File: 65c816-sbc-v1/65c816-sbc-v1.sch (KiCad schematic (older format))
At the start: 13 parts, among them U1 W65C816SxP, U10 W65C22SxP, U2 74HC573, U3 74HC245, U4 PAL20L8, U5 PAL20L8, U6 74HC244, U7 74HC244, U8 AS6C4008-55PCN, U9 28C256

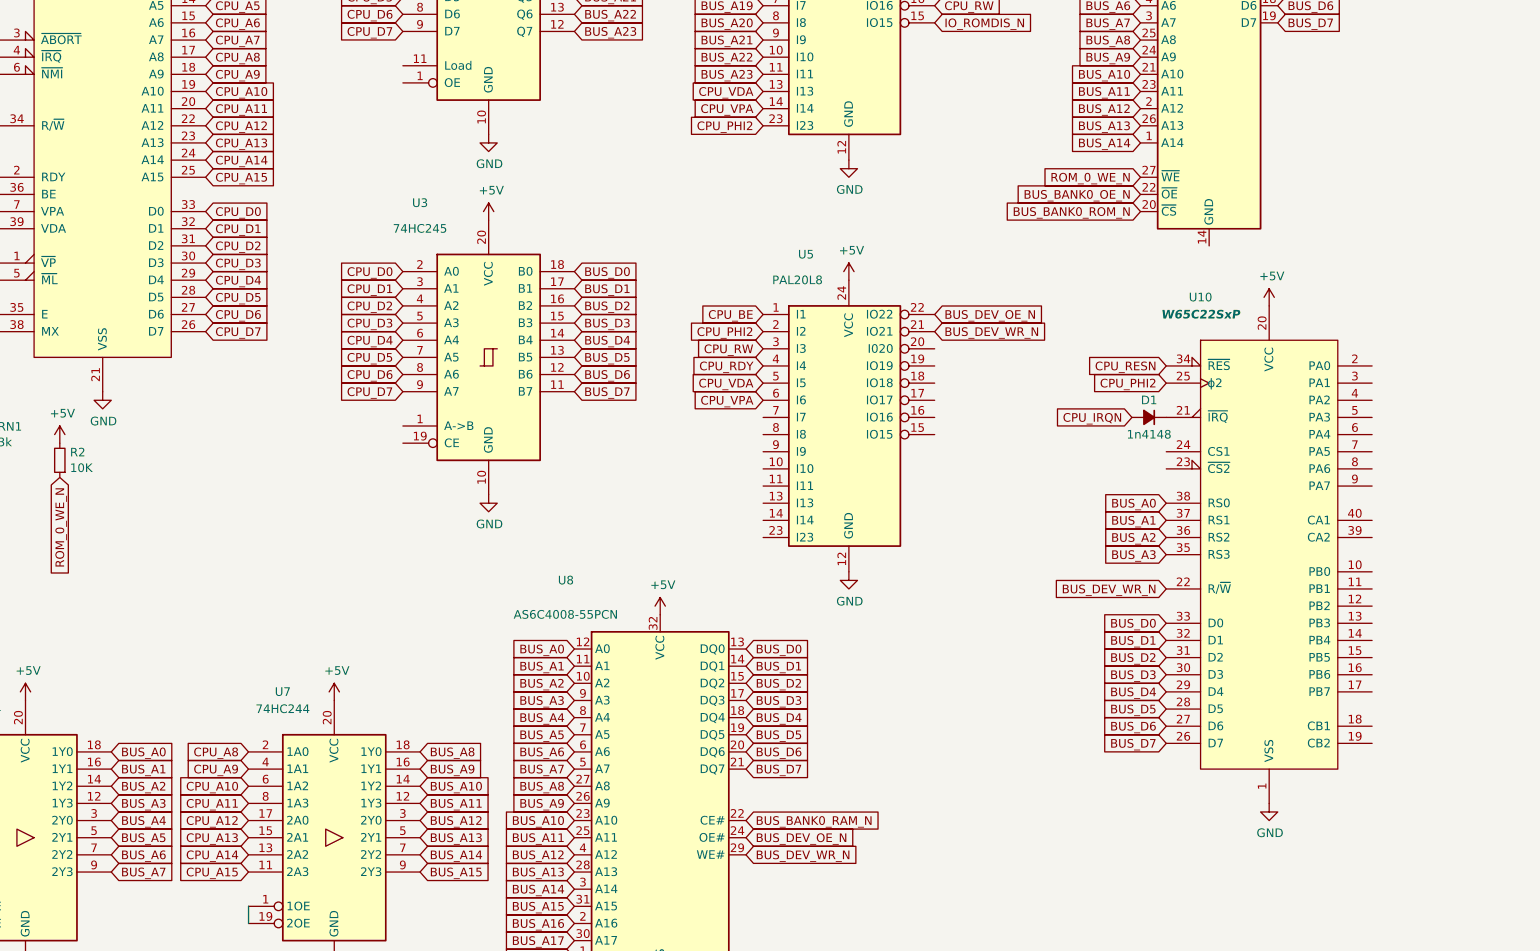
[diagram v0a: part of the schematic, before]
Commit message: squeeze in an ACIA too
It's half done, and I still need to figur eout how to do the two CS'es
on these peripherals given my current IO decoding scheme.
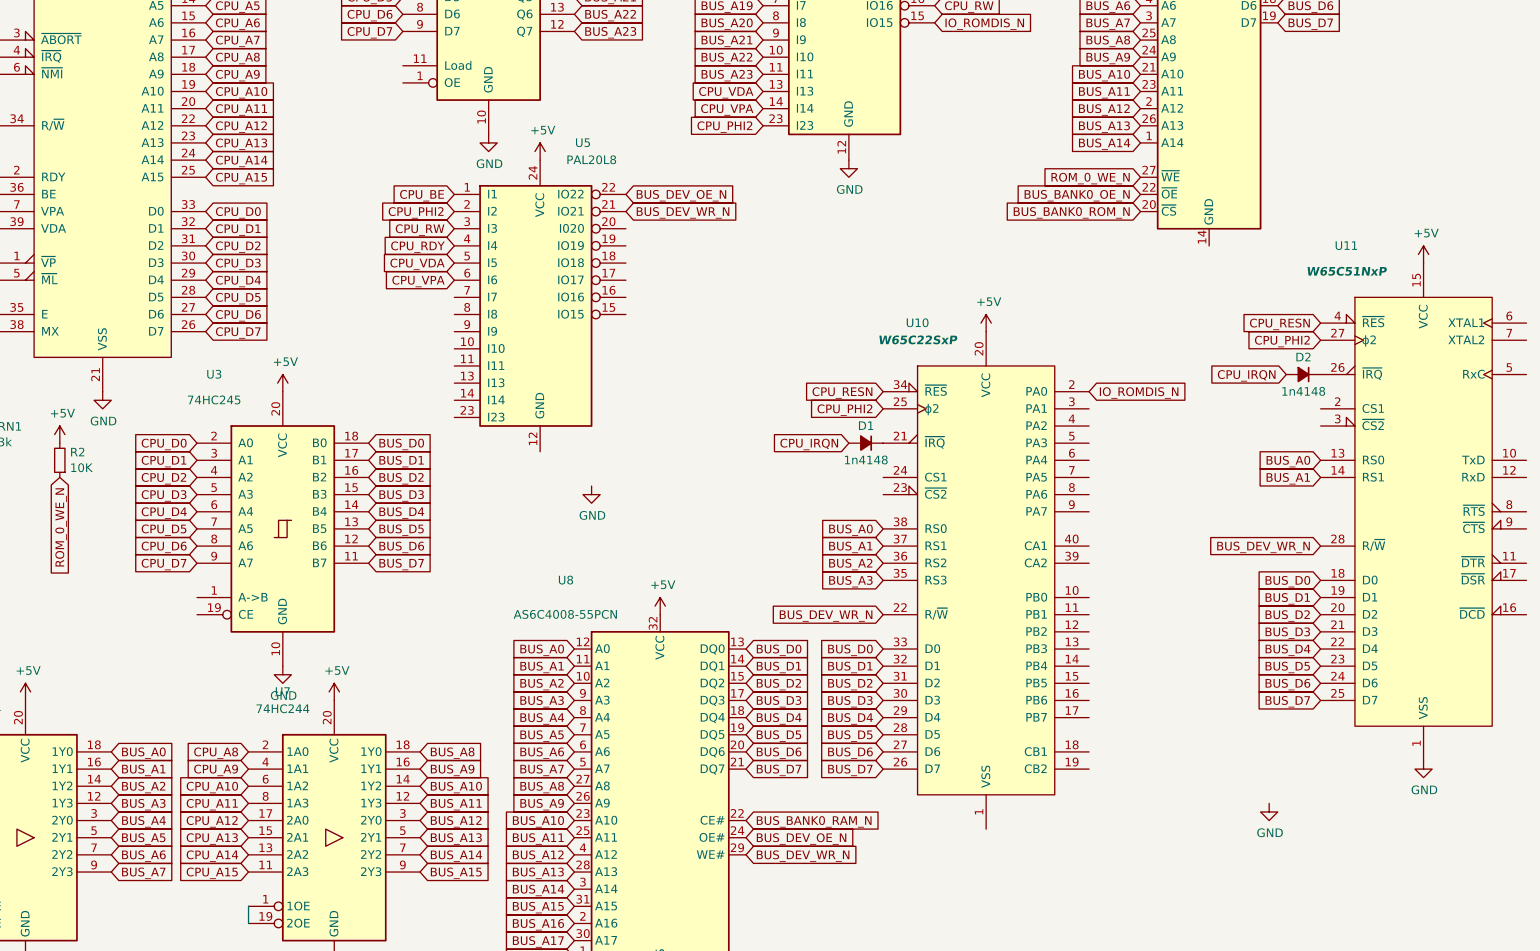
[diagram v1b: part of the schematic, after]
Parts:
- added D2: 1n4148, symbol Device:D_Small_ALT
- added U11: W65C51NxP, symbol 65xx:W65C51NxP
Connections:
- net +5V: now also U11.15 (VCC)
- net BUS_A0: now also U11.13 (RS0)
- net BUS_A1: now also U11.14 (RS1)
- net BUS_D0: now also U11.18 (D0)
- net BUS_D1: now also U11.19 (D1)
- net BUS_D2: now also U11.20 (D2)
- net BUS_D3: now also U11.21 (D3)
- net BUS_D4: now also U11.22 (D4)
- net BUS_D5: now also U11.23 (D5)
- net BUS_D6: now also U11.24 (D6)
- net BUS_D7: now also U11.25 (D7)
- net BUS_DEV_WR_N: now also U11.28 (R/~W)
- net CPU_IRQN: now also D2.2 (A)
- net CPU_PHI2: now also U11.27 (ϕ2)
- net CPU_RESN: now also U11.4 (~RES)
- net GND: now also U11.1 (VSS); no longer U10.1 (VSS), U5.12 (GND)
- net IO_ROMDIS_N: now also U10.2 (PA0)
- new net: D2.1 (K), U11.26 (~IRQ)
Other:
- moved on the sheet: D1, U10, U3, U5

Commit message: Update larger layout, more IO pins defined
Still need to do clock, reset sequencing, etc.
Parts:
- added C1: 30pF, symbol Device:C_Small
- added R3: 1M, symbol Device:R_Small
- added U12: 74HC138, symbol 74xx:74LS138
- added Y1: 1.8432MHz, symbol Device:Crystal
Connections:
- net +5V: now also U9.28 (VCC), U12.16 (VCC); no longer U3.20 (VCC)
- net BUS_A4: now also U12.1 (A0)
- net BUS_A5: now also U12.2 (A1)
- net BUS_A6: now also U12.3 (A2)
- net BUS_A7: now also U12.6 (E3)
- net BUS_A8: now also U12.5 (E2)
- net BUS_BANK0_IO_N: now also U12.4 (E1)
- net GND: now also U10.1 (VSS), U5.12 (GND), U9.14 (GND), C1.2, U12.8 (GND)
- net BUS_DA_LATCH_OE_N: now reaches U2.1 (OE)
- net BUS_DA_LATCH_OE_N: now also U3.19 (CE), U5.15 (IO15), U6.1 (1OE), U6.19 (2OE), U7.1 (1OE), U7.19 (2OE)
- net BUS_DA_LATCH_LE: now reaches U2.11 (Load)
- net BUS_DA_LATCH_LE: now also U5.16 (IO16)
- net BUS_DA_LATCH_DIR: now reaches U3.1 (A->B)
- net BUS_DA_LATCH_DIR: now also U5.17 (IO17)
- net BUS_IO_DEVICE_EN: now reaches U11.2 (CS1)
- net BUS_IO_DEVICE_EN: now also U10.24 (CS1), U5.20 (I020)
- net IO_CSEN_0_N: now reaches U11.3 (~CS2)
- net IO_CSEN_0_N: now also U12.15 (O0)
- net ACIA_XTAL1: now reaches U11.6 (XTAL1)
- net ACIA_XTAL1: now also R3.1, Y1.1
- net ACIA_XTAL2: now reaches U11.7 (XTAL2)
- net ACIA_XTAL2: now also C1.1, R3.2, Y1.2
- net IO_CSEN_1_N: now reaches U10.23 (~CS2)
- net IO_CSEN_1_N: now also U12.14 (O1)
- new net IO_CSEN_2_N: U12.13 (O2)
- new net IO_CSEN_3_N: U12.12 (O3)
- new net IO_CSEN_4_N: U12.11 (O4)
- new net IO_CSEN_5_N: U12.10 (O5)
- new net IO_CSEN_6_N: U12.9 (O6)
- new net IO_CSEN_7_N: U12.7 (O7)
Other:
- moved on the sheet: D1, D2, R2, RN1, U10, U11, U2, U3, U4, U5, U6, U7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

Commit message: starting to play around with buttons
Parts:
- added C3: 1uF, symbol Device:C_Small
- added D3: 1N4148, symbol Device:D_Small
- added R8: 2M, symbol Device:R_Small
- added SW1: RESET, symbol Switch:SW_Push
- added SW2: NMI, symbol Switch:SW_Push
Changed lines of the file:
@@
 Text GLabel 12050 6050 0    50   Input ~ 0
 BUS_IO_DEVICE_EN
+$Comp
+L Device:D_Small D3
+U 1 1 61DCFAE9
+P 14000 3950
+F 0 "D3" H 14000 4157 50  0000 C CNN
+F 1 "1N4148" H 14000 4066 50  0000 C CNN
+F 2 "" V 14000 3950 50  0001 C CNN
+F 3 "~" V 14000 3950 50  0001 C CNN
+	1    14000 3950
+	1    0    0    -1
+$EndComp
+$Comp
+L Device:R_Small R8
+U 1 1 61DD0317
+P 14000 4300
+F 0 "R8" V 14196 4300 50  0000 C CNN
+F 1 "2M" V 14105 4300 50  0000 C CNN
+F 2 "" H 14000 4300 50  0001 C CNN
+F 3 "~" H 14000 4300 50  0001 C CNN
+	1    14000 4300
+	0    -1   -1   0
+$EndComp
+$Comp
+L Device:C_Small C3
+U 1 1 61DD0F01
+P 14450 4050
+F 0 "C3" H 14542 4096 50  0000 L CNN
+F 1 "1uF" H 14542 4005 50  0000 L CNN
+F 2 "" H 14450 4050 50  0001 C CNN
+F 3 "~" H 14450 4050 50  0001 C CNN
+	1    14450 4050
+	1    0    0    -1
+$EndComp
+$Comp
+L Switch:SW_Push SW1
+U 1 1 61DD2E7B
+P 15500 4400
+F 0 "SW1" H 15500 4685 50  0000 C CNN
+F 1 "RESET" H 15500 4594 50  0000 C CNN
+F 2 "" H 15500 4600 50  0001 C CNN
+F 3 "~" H 15500 4600 50  0001 C CNN
+	1    15500 4400
+	1    0    0    -1
+$EndComp
+$Comp
+L Switch:SW_Push SW2
+U 1 1 61DD3596
+P 15450 4850
+F 0 "SW2" H 15450 5135 50  0000 C CNN
+F 1 "NMI" H 15450 5044 50  0000 C CNN
+F 2 "" H 15450 5050 50  0001 C CNN
+F 3 "~" H 15450 5050 50  0001 C CNN
+	1    15450 4850
+	1    0    0    -1
+$EndComp
 $EndSCHEMATC

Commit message: More routing!
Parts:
- added C20, C21, C22, C23, C24, C25, C26, C27, C28, C29, C30, C31: 0.1u, symbol Device:C_Small
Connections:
- net +5V: now also U3.20 (VCC), C20.1, C21.1, C22.1, C23.1, C24.1, C25.1, C26.1, C27.1, C28.1, C29.1, C30.1, C31.1
- net GND: now also C20.2, C21.2, C22.2, C23.2, C24.2, C25.2, C26.2, C27.2, C28.2, C29.2, C30.2, C31.2
- net ACIA_TXD: now reaches U11.10 (TxD)
- net ACIA_DTR: now reaches U11.11 (~DTR)
- net ACIA_RXD: now reaches U11.12 (RxD)
- net ACIA_DCD: now reaches U11.16 (~DCD)
- net ACIA_DSR: now reaches U11.17 (~DSR)
- net ACIA_RXC: now reaches U11.5 (RxC)
- net ACIA_RTS: now reaches U11.8 (~RTS)
- net ACIA_CTS: now reaches U11.9 (~CTS)
- net VIA_PB0: now reaches U10.10 (PB0)
- net VIA_PB1: now reaches U10.11 (PB1)
- net VIA_PB2: now reaches U10.12 (PB2)
- net VIA_PB3: now reaches U10.13 (PB3)
- net VIA_PB4: now reaches U10.14 (PB4)
- net VIA_PB5: now reaches U10.15 (PB5)
- net VIA_PB6: now reaches U10.16 (PB6)
- net VIA_PB7: now reaches U10.17 (PB7)
- net VIA_CB1: now reaches U10.18 (CB1)
- net VIA_CB2: now reaches U10.19 (CB2)
- net VIA_PA1: now reaches U10.3 (PA1)
- net VIA_CA2: now reaches U10.39 (CA2)
- net VIA_PA2: now reaches U10.4 (PA2)
- net VIA_CA1: now reaches U10.40 (CA1)
- net VIA_PA3: now reaches U10.5 (PA3)
- net VIA_PA4: now reaches U10.6 (PA4)
- net VIA_PA5: now reaches U10.7 (PA5)
- net VIA_PA6: now reaches U10.8 (PA6)
- net VIA_PA7: now reaches U10.9 (PA7)

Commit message: * update * add some microchip/AVR GAL symbols to maybe start using
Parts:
- added J1: EXPANSION, symbol Connector_Generic:Conn_02x20_Counter_Clockwise
- added J2: SIO, symbol Connector_Generic:Conn_02x10_Counter_Clockwise
- added J3: VIA_A, symbol Connector:Conn_01x10_Male
- added J4: VIA_B, symbol Connector:Conn_01x10_Male
- added U15: 74HC74, symbol 74xx:74HC74
- added X1: 28MHz, Oscillator:Oscillator_DIP-14, symbol Oscillator:CXO_DIP14
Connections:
- net +5V: now also J1.1 (Pin_1), J2.1 (Pin_1), U15.1 (~R), U15.14 (VCC), U15.4 (~S), X1.14 (Vcc)
- net ACIA_CTS: now also J2.16 (Pin_16)
- net ACIA_DCD: now also J2.13 (Pin_13)
- net ACIA_DSR: now also J2.14 (Pin_14)
- net ACIA_DTR: now also J2.15 (Pin_15)
- net ACIA_RTS: now also J2.17 (Pin_17)
- net ACIA_RXD: now also J2.18 (Pin_18)
- net ACIA_TXD: now also J2.19 (Pin_19)
- net BUS_A0: now also J1.2 (Pin_2)
- net BUS_A1: now also J1.3 (Pin_3)
- net BUS_A10: now also J1.12 (Pin_12)
- net BUS_A11: now also J1.13 (Pin_13)
- net BUS_A12: now also J1.14 (Pin_14)
- net BUS_A13: now also U4.2 (I2), J1.15 (Pin_15); no longer U4.1 (I1)
- net BUS_A14: now also U4.3 (I3), J1.16 (Pin_16); no longer U4.2 (I2)
- net BUS_A15: now also U4.4 (I4), J1.17 (Pin_17); no longer U4.3 (I3)
- net BUS_A16: now also U4.5 (I5), J1.18 (Pin_18); no longer U4.4 (I4)
- net BUS_A17: now also U4.6 (I6), J1.19 (Pin_19); no longer U4.5 (I5)
- net BUS_A18: now also U4.7 (I7), J1.20 (Pin_20); no longer U4.6 (I6)
- net BUS_A19: now also U4.8 (I8), J1.21 (Pin_21); no longer U4.7 (I7)
- net BUS_A2: now also J1.4 (Pin_4)
- net BUS_A20: now also U4.9 (I9), J1.22 (Pin_22); no longer U4.8 (I8)
- net BUS_A21: now also U4.10 (I10), J1.23 (Pin_23); no longer U4.9 (I9)
- net BUS_A22: now also U4.11 (I11), J1.24 (Pin_24); no longer U4.10 (I10)
- net BUS_A23: now also U4.13 (I13), J1.25 (Pin_25); no longer U4.11 (I11)
- net BUS_A3: now also J1.5 (Pin_5)
- net BUS_A4: now also J1.6 (Pin_6)
- net BUS_A5: now also J1.7 (Pin_7)
- net BUS_A6: now also J1.8 (Pin_8)
- net BUS_A7: now also J1.9 (Pin_9)
- net BUS_A8: now also J1.10 (Pin_10)
- net BUS_A9: now also J1.11 (Pin_11)
- net BUS_D0: now also J1.36 (Pin_36)
- net BUS_D1: now also J1.35 (Pin_35)
- net BUS_D2: now also J1.34 (Pin_34)
- net BUS_D3: now also J1.33 (Pin_33)
- net BUS_D4: now also J1.32 (Pin_32)
- net BUS_D5: now also J1.31 (Pin_31)
- net BUS_D6: now also J1.30 (Pin_30)
- net BUS_D7: now also J1.29 (Pin_29)
- net BUS_DEV_OE_N: now also J1.28 (Pin_28)
- net BUS_DEV_WR_N: now also J1.27 (Pin_27)
- net CPU_BE: now also U5.2 (I2); no longer U5.1 (I1)
- net CPU_PHI2: now also U4.1 (I1), U5.1 (I1), J1.38 (Pin_38), U15.5 (Q); no longer U4.23 (I23), U5.2 (I2)
- net CPU_RESN: now also J1.37 (Pin_37), J2.11 (Pin_11)
- net CPU_VDA: now also U4.14 (I14); no longer U4.13 (I13)
- net CPU_VPA: now also U4.23 (I23); no longer U4.14 (I14)
- net GND: now also J1.40 (Pin_40), J2.20 (Pin_20), U15.7 (GND), X1.7 (GND)
- net IO_ROMDIS_N: now also J3.1 (Pin_1)
- net VIA_CA1: now also J3.9 (Pin_9)
- net VIA_CA2: now also J3.10 (Pin_10)
- net VIA_CB1: now also J4.9 (Pin_9)
- net VIA_CB2: now also J4.10 (Pin_10)
- net VIA_PA1: now also J3.2 (Pin_2)
- net VIA_PA2: now also J3.3 (Pin_3)
- net VIA_PA3: now also J3.4 (Pin_4)
- net VIA_PA4: now also J3.5 (Pin_5)
- net VIA_PA5: now also J3.6 (Pin_6)
- net VIA_PA6: now also J3.7 (Pin_7)
- net VIA_PA7: now also J3.8 (Pin_8)
- net VIA_PB0: now also J4.1 (Pin_1)
- net VIA_PB1: now also J4.2 (Pin_2)
- net VIA_PB2: now also J4.3 (Pin_3)
- net VIA_PB3: now also J4.4 (Pin_4)
- net VIA_PB4: now also J4.5 (Pin_5)
- net VIA_PB5: now also J4.6 (Pin_6)
- net VIA_PB6: now also J4.7 (Pin_7)
- net VIA_PB7: now also J4.8 (Pin_8)
- new net: U15.3 (C), X1.8 (OUT)
- new net BUS_A24: J1.26 (Pin_26)
- new net CPU_PHI1: J1.39 (Pin_39), U15.2 (D), U15.6 (~Q)
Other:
- moved on the sheet: D1, U10, U8

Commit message: update!
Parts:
- added C32, C33, C34, C35, C36, C37: 0.1u, symbol Device:C_Small
- added C38: 33uF, symbol Device:CP
- added J5: power, symbol Connector:Conn_01x02_Male
- D1, D2, D3: footprint (none) -> Diode_THT:D_DO-35_SOD27_P7.62mm_Horizontal
- J1: footprint (none) -> Connector_PinHeader_2.54mm:PinHeader_2x20_P2.54mm_Vertical
- J2: footprint (none) -> Connector_PinHeader_2.54mm:PinHeader_2x10_P2.54mm_Vertical
- J3, J4: footprint (none) -> Connector_PinHeader_2.54mm:PinHeader_1x10_P2.54mm_Vertical
- U1, U10, U11: footprint (none) -> Package_DIP:DIP-40_W25.4mm_Socket
- U12: footprint (none) -> Package_DIP:DIP-16_W7.62mm_Socket
- U15: footprint (none) -> Package_DIP:DIP-14_W7.62mm_Socket
- U2, U3, U6, U7: footprint (none) -> Package_DIP:DIP-20_W7.62mm_Socket
- U4, U5: footprint (none) -> Package_DIP:DIP-24_W15.24mm_Socket
- U9: footprint (none) -> Package_DIP:DIP-28_W7.62mm_Socket
- Y1: footprint (none) -> Crystal:Crystal_HC49-4H_Vertical
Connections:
- net +5V: now also D3.1 (K), R8.1, C32.1, C33.1, C34.1, C35.1, C36.1, C37.1, C38.1, J5.1 (Pin_1)
- net CPU_NMIN: now also SW2.1
- net CPU_RESN: now also C3.1, SW1.2
- net GND: now also C3.2, SW2.2, C32.2, C33.2, C34.2, C35.2, C36.2, C37.2, C38.2, J5.2 (Pin_2)
- net at D3.2 (A): now also R8.2, SW1.1
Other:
- moved on the sheet: C3, D3, R8, SW1, SW2
